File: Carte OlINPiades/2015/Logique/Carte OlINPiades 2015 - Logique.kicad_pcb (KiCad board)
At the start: 2 copper layers, 30 parts, among them U1 dsPIC33FJ128MC802, U2 LM7805, U3 LM2937-3.3

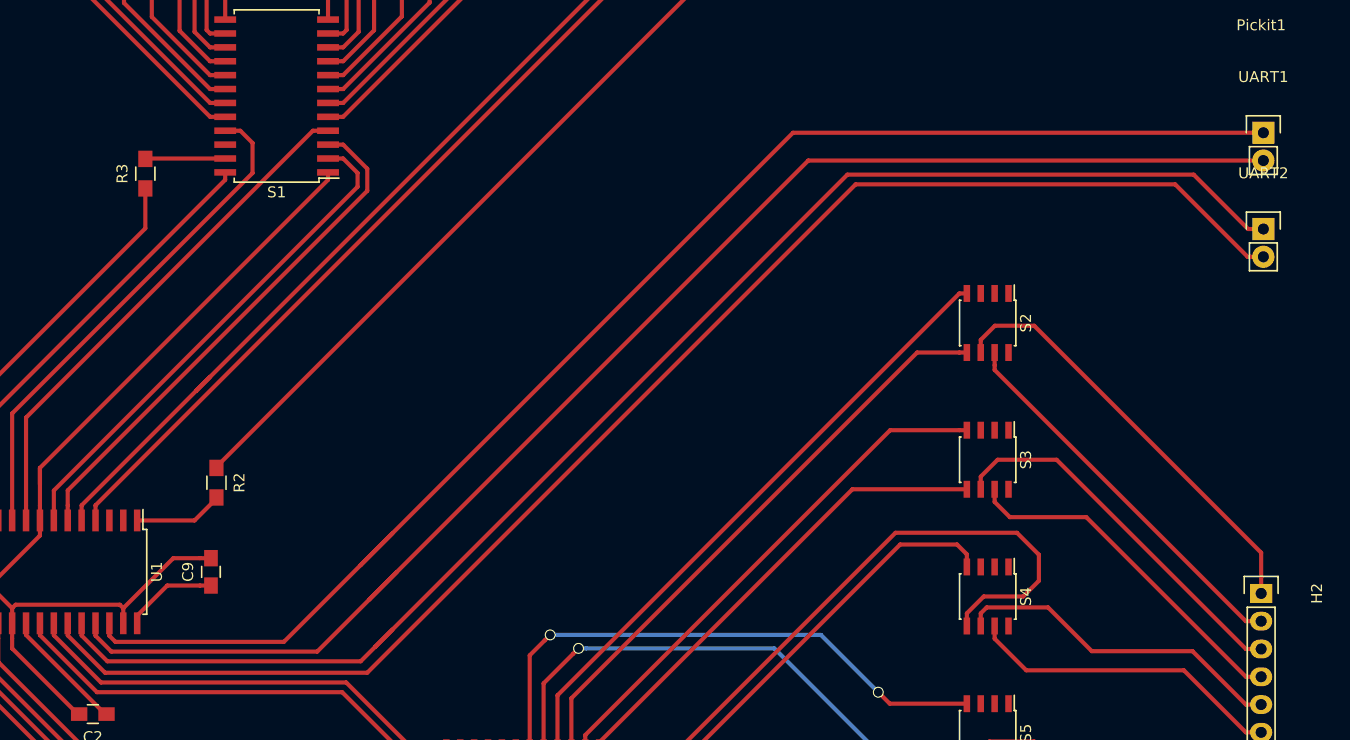
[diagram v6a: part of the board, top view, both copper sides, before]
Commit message: déplace connecteurs UART
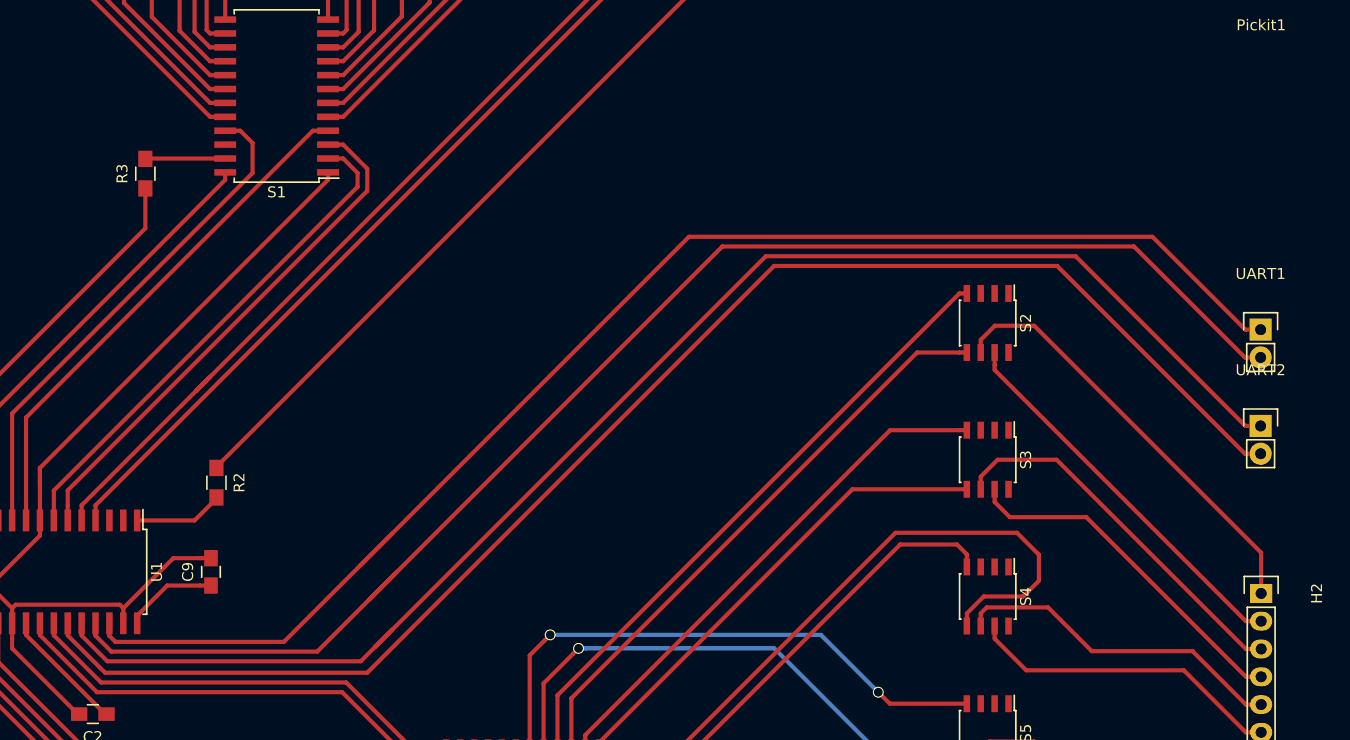
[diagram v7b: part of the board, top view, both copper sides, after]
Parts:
- moved UART1 18.0 mm to (229.9, 56.9)
- moved UART2 18.0 mm to (229.9, 65.7)
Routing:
- net RB13: track 132.9 -> 133.9 mm
- net RB12: track 133.1 -> 134.1 mm
- net RB14: track 130.6 -> 131.3 mm
- net RB15: track 130.3 -> 129.6 mm
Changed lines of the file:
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@@
     (thickness 1.6)
     (drawings 6)
-    (tracks 432)
+    (tracks 436)
     (zones 0)
     (modules 30)
@@
   )
   (module Pin_Headers:Pin_Header_Straight_1x02 (layer F.Cu)
-    (at 230.2 38.86)
+    (at 229.95 56.86)
     (descr "Through hole pin header")
     (tags "pin header")
@@
   )
   (module Pin_Headers:Pin_Header_Straight_1x02 (layer F.Cu)
-    (at 230.2 47.66)
+    (at 229.95 65.66)
     (descr "Through hole pin header")
     (tags "pin header")
@@
   (segment (start 154.405447 97.154945) (end 156.311055 97.154945) (width 0.381) (layer F.Cu) (net 42))
   (segment (start 119.635 83.7) (end 119.635 84.795498) (width 0.381) (layer F.Cu) (net 42))
-  (segment (start 230.2 50.2) (end 228.76316 50.2) (width 0.381) (layer F.Cu) (net 43))
-  (segment (start 124.31873 88.221978) (end 148.284773 88.221978) (width 0.381) (layer F.Cu) (net 43))
-  (segment (start 228.76316 50.2) (end 222.139659 43.576499) (width 0.381) (layer F.Cu) (net 43))
-  (segment (start 222.139659 43.576499) (end 192.930252 43.576499) (width 0.381) (layer F.Cu) (net 43))
-  (segment (start 192.930252 43.576499) (end 148.284773 88.221978) (width 0.381) (layer F.Cu) (net 43))
-  (segment (start 120.905 84.808248) (end 124.31873 88.221978) (width 0.381) (layer F.Cu) (net 43))
-  (segment (start 120.905 83.7) (end 120.905 84.808248) (width 0.381) (layer F.Cu) (net 43))
-  (segment (start 192.175512 42.687488) (end 148.999805 85.863195) (width 0.381) (layer F.Cu) (net 44))
-  (segment (start 228.803 47.66) (end 223.830488 42.687488) (width 0.381) (layer F.Cu) (net 44))
-  (segment (start 230.2 47.66) (end 228.803 47.66) (width 0.381) (layer F.Cu) (net 44))
-  (segment (start 223.830488 42.687488) (end 192.175512 42.687488) (width 0.381) (layer F.Cu) (net 44))
+  (segment (start 120.905 84.808248) (end 120.905 83.7) (width 0.381) (layer F.Cu) (net 43))
+  (segment (start 124.31873 88.221978) (end 120.905 84.808248) (width 0.381) (layer F.Cu) (net 43))
+  (segment (start 185.471868 51.034883) (end 148.284773 88.221978) (width 0.381) (layer F.Cu) (net 43))
+  (segment (start 211.348043 51.034883) (end 185.471868 51.034883) (width 0.381) (layer F.Cu) (net 43))
+  (segment (start 228.51316 68.2) (end 211.348043 51.034883) (width 0.381) (layer F.Cu) (net 43))
+  (segment (start 229.95 68.2) (end 228.51316 68.2) (width 0.381) (layer F.Cu) (net 43))
+  (segment (start 148.284773 88.221978) (end 124.31873 88.221978) (width 0.381) (layer F.Cu) (net 43))
+  (segment (start 213.038872 50.145872) (end 184.717128 50.145872) (width 0.381) (layer F.Cu) (net 44))
+  (segment (start 184.717128 50.145872) (end 148.999805 85.863195) (width 0.381) (layer F.Cu) (net 44))
+  (segment (start 229.95 65.66) (end 228.553 65.66) (width 0.381) (layer F.Cu) (net 44))
+  (segment (start 228.553 65.66) (end 213.038872 50.145872) (width 0.381) (layer F.Cu) (net 44))
   (segment (start 147.686478 87.176522) (end 148.999805 85.863195) (width 0.381) (layer F.Cu) (net 44))
   (segment (start 148.999805 85.863195) (end 150.603 84.26) (width 0.381) (layer F.Cu) (net 44))
@@
   (segment (start 122.175 83.7) (end 122.175 84.820998) (width 0.381) (layer F.Cu) (net 44))
   (segment (start 124.530524 87.176522) (end 147.686478 87.176522) (width 0.381) (layer F.Cu) (net 44))
-  (segment (start 230.2 41.4) (end 188.6 41.4) (width 0.381) (layer F.Cu) (net 45))
-  (segment (start 188.6 41.4) (end 148.472483 81.527517) (width 0.381) (layer F.Cu) (net 45))
+  (segment (start 180.743139 49.256861) (end 148.472483 81.527517) (width 0.381) (layer F.Cu) (net 45))
+  (segment (start 228.51316 59.4) (end 218.370021 49.256861) (width 0.381) (layer F.Cu) (net 45))
+  (segment (start 218.370021 49.256861) (end 180.743139 49.256861) (width 0.381) (layer F.Cu) (net 45))
+  (segment (start 229.95 59.4) (end 228.51316 59.4) (width 0.381) (layer F.Cu) (net 45))
   (segment (start 143.712489 86.287511) (end 148.472483 81.527517) (width 0.381) (layer F.Cu) (net 45))
   (segment (start 148.472483 81.527517) (end 150.984001 79.015999) (width 0.381) (layer F.Cu) (net 45))
@@
   (segment (start 123.445 84.833748) (end 124.898763 86.287511) (width 0.381) (layer F.Cu) (net 45))
   (segment (start 123.445 83.7) (end 123.445 84.833748) (width 0.381) (layer F.Cu) (net 45))
+  (segment (start 229.95 56.86) (end 228.553 56.86) (width 0.381) (layer F.Cu) (net 46))
+  (segment (start 228.553 56.86) (end 220.06085 48.36785) (width 0.381) (layer F.Cu) (net 46))
+  (segment (start 220.06085 48.36785) (end 177.69515 48.36785) (width 0.381) (layer F.Cu) (net 46))
+  (segment (start 177.69515 48.36785) (end 147.667648 78.395352) (width 0.381) (layer F.Cu) (net 46))
   (segment (start 140.6645 85.3985) (end 147.667648 78.395352) (width 0.381) (layer F.Cu) (net 46))
   (segment (start 147.667648 78.395352) (end 150.603 75.46) (width 0.381) (layer F.Cu) (net 46))
-  (segment (start 230.2 38.86) (end 187.203 38.86) (width 0.381) (layer F.Cu) (net 46))
-  (segment (start 187.203 38.86) (end 147.667648 78.395352) (width 0.381) (layer F.Cu) (net 46))
   (segment (start 124.715 84.846498) (end 125.267002 85.3985) (width 0.381) (layer F.Cu) (net 46))
   (segment (start 125.267002 85.3985) (end 140.6645 85.3985) (width 0.381) (layer F.Cu) (net 46))

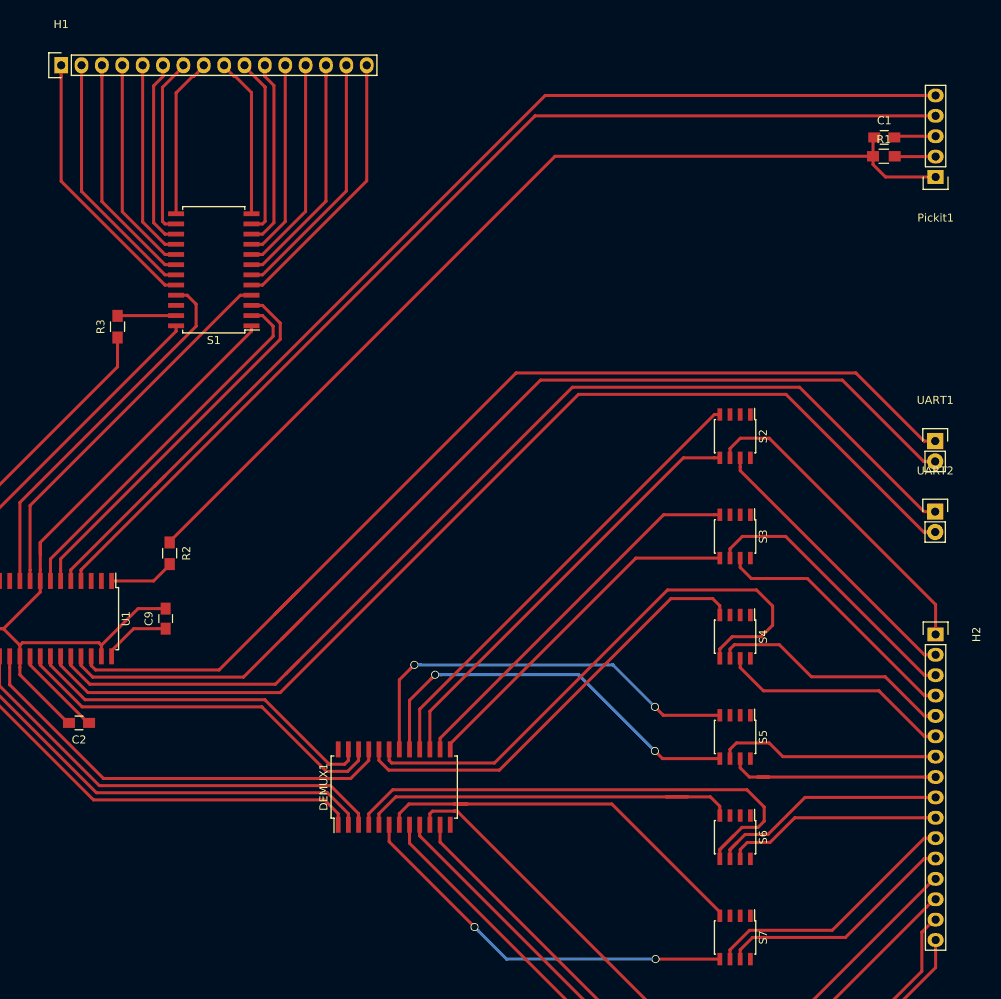
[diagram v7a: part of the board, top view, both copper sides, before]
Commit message: change la face des pins receptrice de la matrice de leds
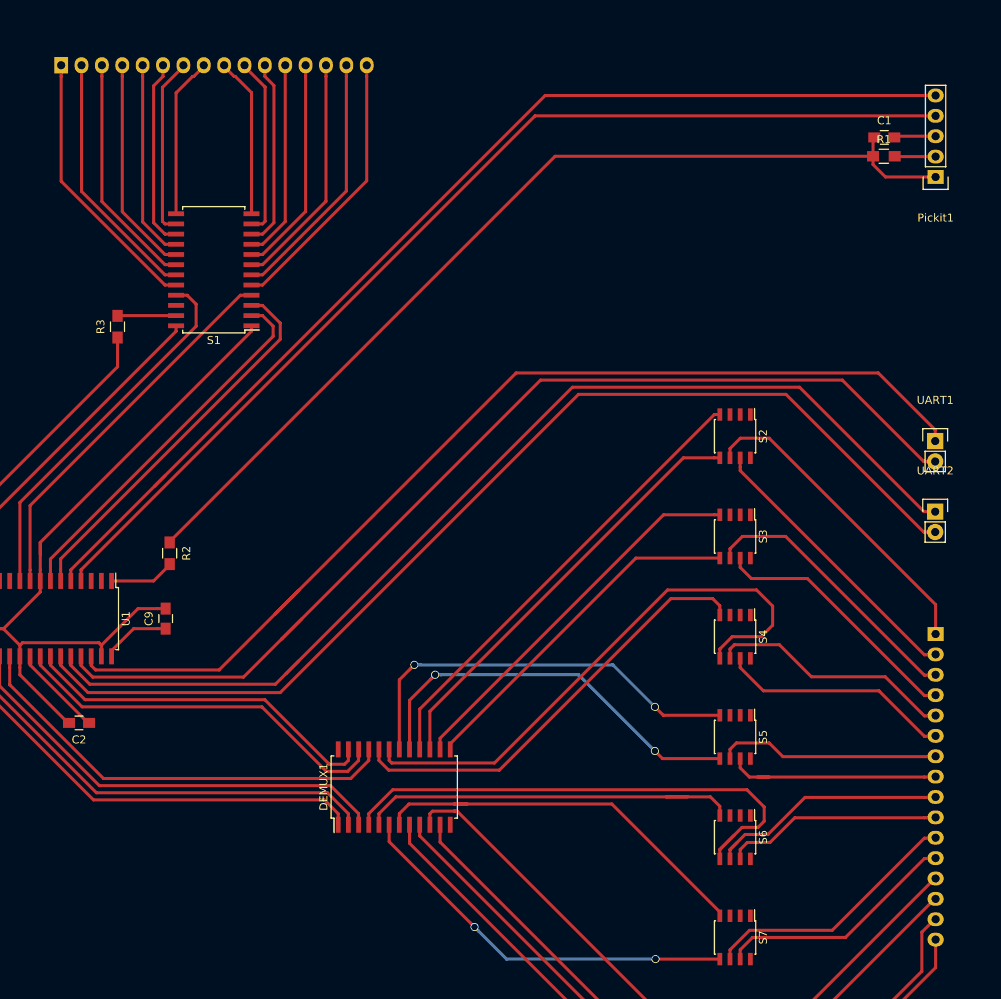
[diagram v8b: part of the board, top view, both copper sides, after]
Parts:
- H1, H2: moved to B.Cu
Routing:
- net RB15: track 129.6 -> 130.4 mm
